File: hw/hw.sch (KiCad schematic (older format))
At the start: 20 parts, among them U1 74LS299, U2 74LS138, U3 Z80CPU, U4 74LS161, U5 CY7C199, U6 74LS107, X1 CXO_DIP8

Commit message: start to try and rationalise arduino port
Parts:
- added D?: 1N4148, Diode_THT:D_DO-35_SOD27_P7.62mm_Horizontal, symbol Diode:1N4148
- added U? (x3): 74LS32, symbol 74xx:74LS32
- added U? (x3): 74LS74, symbol 74xx:74LS74
- added U? (x5): 74LS08, symbol 74xx:74LS08
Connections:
- net labels added: HSYNC_RAW, ~INTACK, ~M1, ~RAM_REQ, ~REFRESH
- wire segments 224 -> 269
- no-connect marks 33 -> 34
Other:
- moved on the sheet: A1, D1, D?, U1, U2, U3, U4, U5, U?, X1

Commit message: start hw rationalisation
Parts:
- removed D? (x5): 1N4148, Diode_THT:D_DO-35_SOD27_P7.62mm_Horizontal, symbol Diode:1N4148
- removed R?: 47R, symbol Device:R
- removed R?: 4K7, symbol Device:R
- removed U2: 74LS138, symbol 74xx:74LS138
- removed U6: 74LS107, symbol 74xx:74LS107
- removed U?: 74LS08, symbol 74xx:74LS08
- removed U?: 74LS32, symbol 74xx:74LS32
- added BAR1: HDSP-4830_2, Display:HDSP-4830, symbol LED:HDSP-4830_2
- added D2: 1N4148, Diode_THT:D_DO-35_SOD27_P7.62mm_Horizontal, symbol Diode:1N4148
- added J1: Conn_01x01_Female, symbol Connector:Conn_01x01_Female
- added J2: Conn_01x08, symbol Connector_Generic:Conn_01x08
- added R? (x2): 4K7, symbol Device:R
- added RN1: R_Network08_US, Resistor_THT:R_Array_SIP9, symbol Device:R_Network08_US
- added unit 1 of U1
- added U11: 74LS245, symbol 74xx:74LS245
- added unit 3 of U2
- added U6: 74LS138, symbol 74xx:74LS138
- R1: value 47K -> 4K7
- gave numbers to parts that had none: 6
- renumbered R2 to R3, U1 to U7, U4 to U9
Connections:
- net labels added: ~ARD_OVR, ~PORTA_RD
- net labels removed: ~ARD, ~IO_ACK, ~SR_OE
- wire segments 269 -> 291
- no-connect marks 34 -> 39
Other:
- note removed: "BUG: cannot read from Arduino via IO port"
- moved on the sheet: R3, U10A, U10C, U1B, U1D, U1E, U2A, U2E, U4, U7, U8

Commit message: fix rationalised circuit
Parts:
- removed J2: Conn_01x08, symbol Connector_Generic:Conn_01x08
- removed unit 2 of U1
- removed U6: 74LS138, symbol 74xx:74LS138
- added D3, D?: LED, symbol Device:LED
- added RN?: R_Network08_US, Resistor_THT:R_Array_SIP9, symbol Device:R_Network08_US
- added unit 4 of U1
- gave numbers to parts that had none: 2
- renumbered R1 to R2, R2 to R4, R3 to R5, U2 to U1, U3 to U2, U4 to U3, U1 to U4, U7 to U6, U8 to U7, U9 to U8, U11 to U9
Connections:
- net labels added: ARD_OVR, ~HALT
- wire segments 291 -> 284
- no-connect marks 39 -> 30
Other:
- moved on the sheet: BAR1, R2

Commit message: start to generate video signal
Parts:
- removed J1: Conn_01x01_Female, symbol Connector:Conn_01x01_Female
- added U? (x3): 74LS04, symbol 74xx:74LS04
- added U?: 74LS273, symbol 74xx:74LS273
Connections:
- net labels added: INTACK
- wire segments 284 -> 288
- no-connect marks 30 -> 31
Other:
- note added: "FIXME: or refresh!"
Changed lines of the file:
@@
 	10400 9000 10400 9100
 NoConn ~ 11450 9300
-NoConn ~ 11450 9000
 NoConn ~ 11450 8900
 Text GLabel 11550 8800 2    50   Output ~ 0
@@
 Text GLabel 3800 5600 2    50   Output ~ 0
 ~ARD_RD
-Text GLabel 11550 9100 2    50   Output ~ 0
+Text GLabel 11550 9000 2    50   Output ~ 0
 CLK_CHAR
 Wire Wire Line
-	11550 9100 11450 9100
+	11550 9000 11450 9000
 Text GLabel 2400 9600 2    50   Input ~ 0
 CLK_CHAR
@@
 	2400 10200 2300 10200
 Text GLabel 12700 800  0    50   Input ~ 0
-HSYNC
+VSYNC
 Text GLabel 12900 800  2    50   Output ~ 0
 ~INT
@@
 	1    0    0    -1
 $EndComp
-Text GLabel 12400 4100 0    50   Input ~ 0
-~INTACK
 Wire Wire Line
 	12900 3600 12900 3700
-$Comp
-L power:GND #PWR037
-U 1 1 5D42E4CC
-P 12500 3900
-F 0 "#PWR037" H 12500 3650 50  0001 C CNN
-F 1 "GND" H 12505 3727 50  0000 C CNN
-F 2 "" H 12500 3900 50  0001 C CNN
-F 3 "" H 12500 3900 50  0001 C CNN
-	1    12500 3900
-	0    1    1    0
-$EndComp
 Wire Wire Line
 	12600 3900 12500 3900
-Text GLabel 12400 3600 0    50   Input ~ 0
-HSYNC
-Wire Wire Line
-	12400 3600 12900 3600
-Wire Wire Line
-	13200 3900 13400 3900
-Text GLabel 13400 3900 2    50   Output ~ 0
+Wire Wire Line
+	12500 4400 12900 4400
+Wire Wire Line
+	13200 4100 13400 4100
+Text GLabel 13400 4100 2    50   Output ~ 0
 ~WAIT
 $Comp
@@
 	12500 3000 12900 3000
 Wire Wire Line
-	12400 4100 12500 4100
-Wire Wire Line
-	12500 4100 12500 4000
-Wire Wire Line
 	12500 4000 12600 4000
-$Comp
-L power:+5V #PWR038
-U 1 1 5D597F98
-P 12500 4400
-F 0 "#PWR038" H 12500 4250 50  0001 C CNN
-F 1 "+5V" H 12515 4573 50  0000 C CNN
-F 2 "" H 12500 4400 50  0001 C CNN
-F 3 "" H 12500 4400 50  0001 C CNN
-	1    12500 4400
-	1    0    0    -1
-$EndComp
-Wire Wire Line
-	12500 4400 12900 4400
 Wire Wire Line
 	12900 4400 12900 4300
-NoConn ~ 13200 4100
 Text GLabel 4900 3050 0    50   Input ~ 0
 ~RAM_REQ
@@
 	10100 5000 9900 5000
 NoConn ~ 2300 10100
-Text GLabel 3550 10800 0    50   Input ~ 0
-VSYNC
-Wire Wire Line
-	3550 10800 3650 10800
-$Comp
-L Connector:Conn_01x01_Female J1
-U 1 1 5E830B1F
-P 3850 10800
-F 0 "J1" H 3877 10826 50  0000 L CNN
-F 1 "Conn_01x01_Female" H 3877 10735 50  0000 L CNN
-F 2 "" H 3850 10800 50  0001 C CNN
-F 3 "~" H 3850 10800 50  0001 C CNN
-	1    3850 10800
-	1    0    0    -1
-$EndComp
 $Comp
 L 74xx:74LS245 U9
@@
 Wire Wire Line
 	1200 7200 1600 7200
-Text GLabel 2400 9500 2    50   Output ~ 0
+Text GLabel 6400 7300 2    50   Output ~ 0
 ARD_OVR
 Wire Wire Line
-	2400 9500 2300 9500
+	6400 7300 6300 7300
 Wire Wire Line
 	5600 9100 5700 9100
@@
 NoConn ~ 9900 5800
 NoConn ~ 9900 5900
+$Comp
+L 74xx:74LS04 U?
+U 6 1 5F320C52
+P 6000 7300
+F 0 "U?" H 6000 7617 50  0000 C CNN
+F 1 "74LS04" H 6000 7526 50  0000 C CNN
+F 2 "" H 6000 7300 50  0001 C CNN
+F 3 "http://www.ti.com/lit/gpn/sn74LS04" H 6000 7300 50  0001 C CNN
+	6    6000 7300
+	1    0    0    -1
+$EndComp
+$Comp
+L 74xx:74LS04 U?
+U 7 1 5F320D2F
+P 13000 8900
+F 0 "U?" H 13230 8946 50  0000 L CNN
+F 1 "74LS04" H 13230 8855 50  0000 L CNN
+F 2 "" H 13000 8900 50  0001 C CNN
+F 3 "http://www.ti.com/lit/gpn/sn74LS04" H 13000 8900 50  0001 C CNN
+	7    13000 8900
+	1    0    0    -1
+$EndComp
+$Comp
+L power:+5V #PWR?
+U 1 1 5F320E22
+P 13000 8300
+F 0 "#PWR?" H 13000 8150 50  0001 C CNN
+F 1 "+5V" H 13015 8473 50  0000 C CNN
+F 2 "" H 13000 8300 50  0001 C CNN
+F 3 "" H 13000 8300 50  0001 C CNN
+	1    13000 8300
+	1    0    0    -1
+$EndComp
+Wire Wire Line
+	13000 8300 13000 8400
+$Comp
+L power:GND #PWR?
+U 1 1 5F33C45D
+P 13000 9500
+F 0 "#PWR?" H 13000 9250 50  0001 C CNN
+F 1 "GND" H 13005 9327 50  0000 C CNN
+F 2 "" H 13000 9500 50  0001 C CNN
+F 3 "" H 13000 9500 50  0001 C CNN
+	1    13000 9500
+	1    0    0    -1
+$EndComp
+Wire Wire Line
+	13000 9400 13000 9500
+Text GLabel 5600 7300 0    50   Input ~ 0
+~ARD_OVR
+Wire Wire Line
+	5600 7300 5700 7300
+NoConn ~ 2300 9500
+Text GLabel 6400 7900 2    50   Output ~ 0
+INTACK
+Wire Wire Line
+	6400 7900 6300 7900
+$Comp
+L 74xx:74LS04 U?
+U 1 1 5F3C62F6
+P 6000 7900
+F 0 "U?" H 6000 8217 50  0000 C CNN
+F 1 "74LS04" H 6000 8126 50  0000 C CNN
+F 2 "" H 6000 7900 50  0001 C CNN
+F 3 "http://www.ti.com/lit/gpn/sn74LS04" H 6000 7900 50  0001 C CNN
+	1    6000 7900
+	1    0    0    -1
+$EndComp
+Text GLabel 5600 7900 0    50   Input ~ 0
+~INTACK
+Wire Wire Line
+	5600 7900 5700 7900
+$Comp
+L power:+5V #PWR?
+U 1 1 5F4A653E
+P 12900 3600
+F 0 "#PWR?" H 12900 3450 50  0001 C CNN
+F 1 "+5V" H 12915 3773 50  0000 C CNN
+F 2 "" H 12900 3600 50  0001 C CNN
+F 3 "" H 12900 3600 50  0001 C CNN
+	1    12900 3600
+	1    0    0    -1
+$EndComp
+$Comp
+L power:+5V #PWR?
+U 1 1 5F4C2BE8
+P 12500 3900
+F 0 "#PWR?" H 12500 3750 50  0001 C CNN
+F 1 "+5V" H 12515 4073 50  0000 C CNN
+F 2 "" H 12500 3900 50  0001 C CNN
+F 3 "" H 12500 3900 50  0001 C CNN
+	1    12500 3900
+	1    0    0    -1
+$EndComp
+Text GLabel 12500 4400 0    50   Input ~ 0
+HSYNC
+Text GLabel 12500 4000 0    50   Input ~ 0
+INTACK
+NoConn ~ 13200 3900
+NoConn ~ 11450 9100
+$Comp
+L 74xx:74LS273 U?
+U 1 1 5F62F988
+P 6300 5300
+F 0 "U?" H 6050 5950 50  0000 C CNN
+F 1 "74LS273" H 6500 5950 50  0000 C CNN
+F 2 "" H 6300 5300 50  0001 C CNN
+F 3 "http://www.ti.com/lit/gpn/sn74LS273" H 6300 5300 50  0001 C CNN
+	1    6300 5300
+	1    0    0    -1
+$EndComp
+$Comp
+L power:+5V #PWR?
+U 1 1 5F62FB90
+P 6300 4400
+F 0 "#PWR?" H 6300 4250 50  0001 C CNN
+F 1 "+5V" H 6315 4573 50  0000 C CNN
+F 2 "" H 6300 4400 50  0001 C CNN
+F 3 "" H 6300 4400 50  0001 C CNN
+	1    6300 4400
+	1    0    0    -1
+$EndComp
+Wire Wire Line
+	6300 4400 6300 4500
+$Comp
+L power:GND #PWR?
+U 1 1 5F64B56F
+P 6300 6200
+F 0 "#PWR?" H 6300 5950 50  0001 C CNN
+F 1 "GND" H 6305 6027 50  0000 C CNN
+F 2 "" H 6300 6200 50  0001 C CNN
+F 3 "" H 6300 6200 50  0001 C CNN
+	1    6300 6200
+	1    0    0    -1
+$EndComp
+Wire Wire Line
+	6300 6100 6300 6200
+$Comp
+L power:+5V #PWR?
+U 1 1 5F66703B
+P 5700 5800
+F 0 "#PWR?" H 5700 5650 50  0001 C CNN
+F 1 "+5V" H 5715 5973 50  0000 C CNN
+F 2 "" H 5700 5800 50  0001 C CNN
+F 3 "" H 5700 5800 50  0001 C CNN
+	1    5700 5800
+	0    -1   -1   0
+$EndComp
+Wire Wire Line
+	5700 5800 5800 5800
+Text Notes 700  8250 0    50   ~ 0
+FIXME: or refresh!
 $EndSCHEMATC

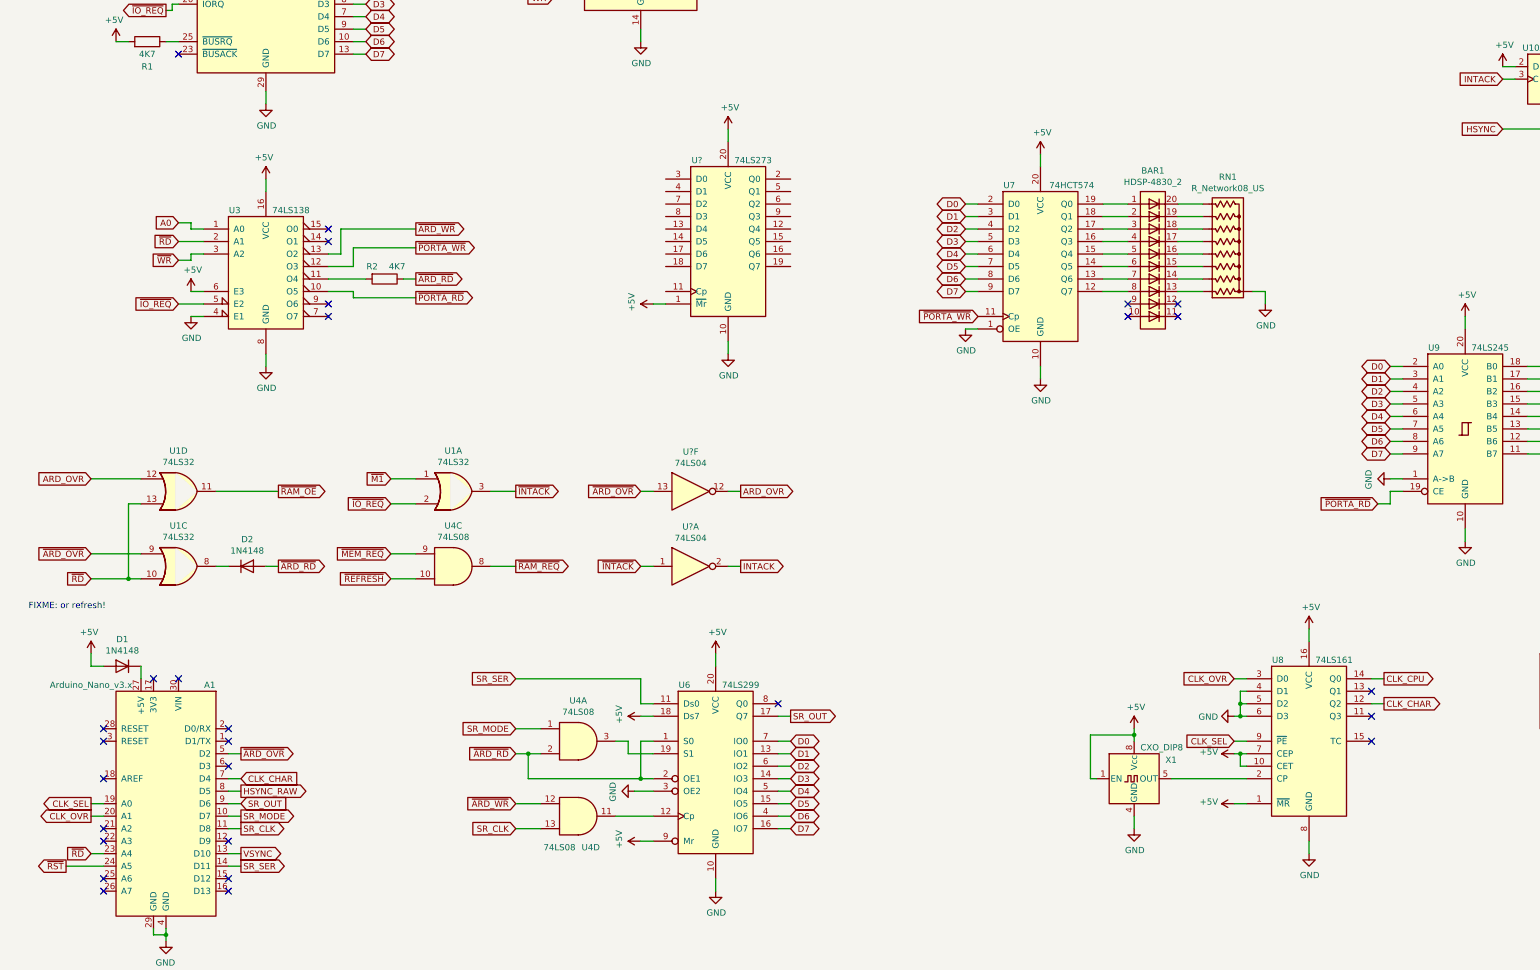
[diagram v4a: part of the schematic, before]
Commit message: start to get per character single pulse
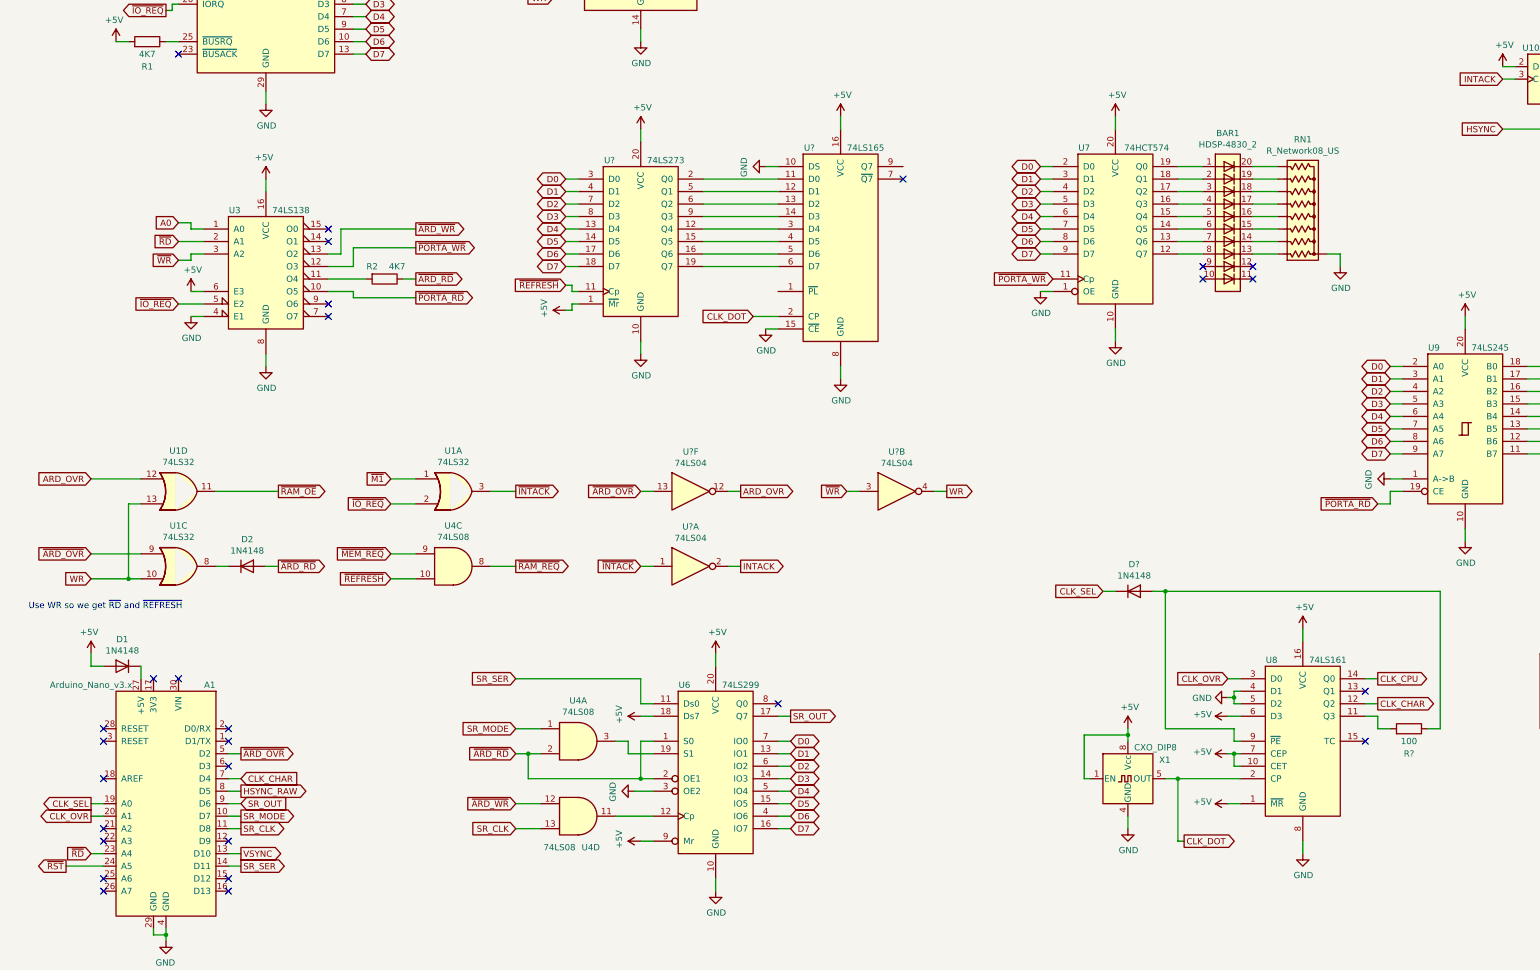
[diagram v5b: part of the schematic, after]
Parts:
- added D?: 1N4148, Diode_THT:D_DO-35_SOD27_P7.62mm_Horizontal, symbol Diode:1N4148
- added R?: 100, symbol Device:R
- added U?: 74LS04, symbol 74xx:74LS04
- added U?: 74LS165, symbol 74xx:74LS165
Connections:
- net +5V: now also U8.6 (D3), U?.16 (VCC)
- net CLK_SEL: now also D?.1 (K); no longer U8.9 (~PE)
- net D0: now also U?.3 (D0)
- net D1: now also U?.4 (D1)
- net D2: now also U?.7 (D2)
- net D3: now also U?.8 (D3)
- net D4: now also U?.13 (D4)
- net D5: now also U?.14 (D5)
- net D6: now also U?.17 (D6)
- net D7: now also U?.18 (D7)
- net GND: now also U?.10 (DS), U?.15 (~CE), U?.8 (GND); no longer U8.6 (D3)
- net ~RD: no longer U1.10, U1.13
- net ~REFRESH: now also U?.11 (Cp)
- net ~WR: now also U?.3
- net CLK_DOT: now reaches U8.2 (CP), X1.5 (OUT)
- net CLK_DOT: now also U?.2 (CP)
- net at U8.11 (Q3): now also R?.2
- net at U?.12 (Q4): now also U?.3 (D4)
- net at U?.15 (Q5): now also U?.4 (D5)
- net at U?.16 (Q6): now also U?.5 (D6)
- net at U?.19 (Q7): now also U?.6 (D7)
- net at U?.2 (Q0): now also U?.11 (D0)
- net at U?.5 (Q1): now also U?.12 (D1)
- net at U?.6 (Q2): now also U?.13 (D2)
- net at U?.9 (Q3): now also U?.14 (D3)
- new net: D?.2 (A), R?.1, U8.9 (~PE)
- new net WR: U1.10, U1.13, U?.4
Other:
- note added: "Use WR so we get ~RD and ~REFRESH"
- note removed: "FIXME: or refresh!"
- moved on the sheet: BAR1, RN1, U7, U8, U?, X1
